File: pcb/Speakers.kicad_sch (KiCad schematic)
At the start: 34 parts, among them J17 Conn_03x01, U4 R_8_ADI, U7 R_8_ADI

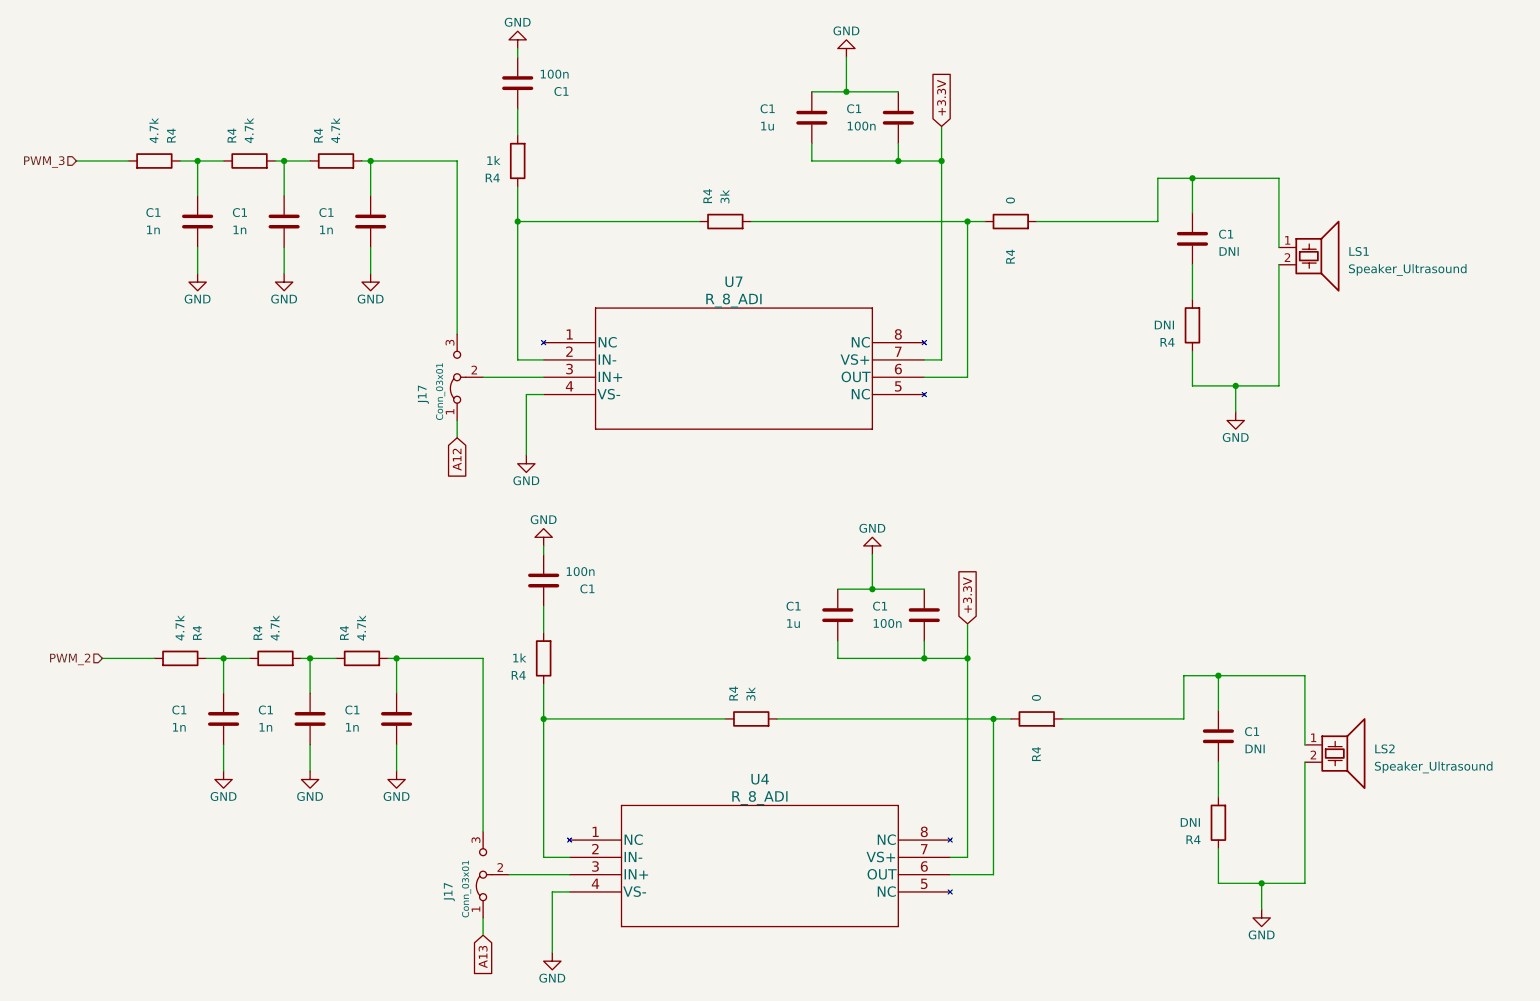
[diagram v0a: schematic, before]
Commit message: feat: Reorganize PCB project
Include all 3D step files
Refactor all folders for symbolds and footprints
Add missing datasheets
Link all symbols in KiCad projects
Rename the project to SensEdu
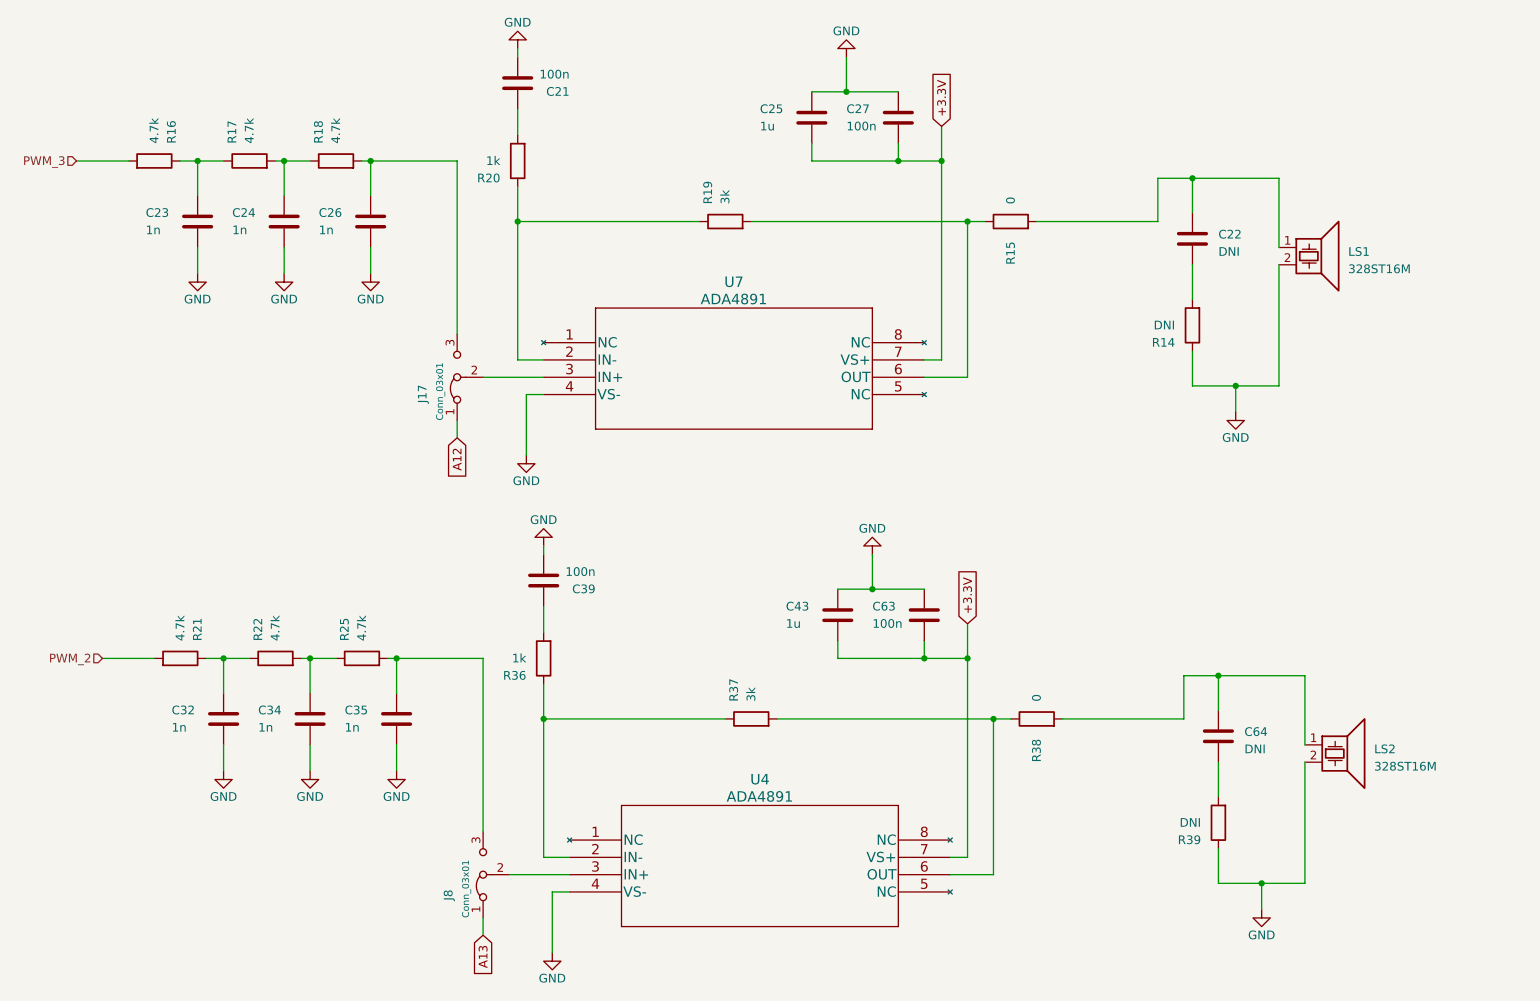
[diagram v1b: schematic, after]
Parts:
- LS1, LS2: value Speaker_Ultrasound -> 328ST16M
- U4, U7: value R_8_ADI -> ADA4891
- renumbered C1 to C21, C1 to C22, C1 to C23, C1 to C24, C1 to C25, C1 to C26, C1 to C27, C1 to C32, C1 to C34, C1 to C35, C1 to C39, C1 to C43, C1 to C63, C1 to C64, J17 to J8, R4 to R14, R4 to R15, R4 to R16, R4 to R17, R4 to R18, R4 to R19, R4 to R20, R4 to R21, R4 to R22, R4 to R25, R4 to R36, R4 to R37, R4 to R38, R4 to R39

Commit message: feat: Fix DRC errors and warnings
Updated footprint links
Updated schematic symbol for LT1790 to remove warnings
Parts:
- LS1, LS2: footprint Speaker:328ST16M_Speaker -> SensEdu:328ST16M_Speaker
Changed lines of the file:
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@@
 			)
 		)
-		(property "Footprint" "Speaker:328ST16M_Speaker"
+		(property "Footprint" "SensEdu:328ST16M_Speaker"
 			(at 209.931 126.365 0)
 			(effects
@@
 			)
 		)
-		(property "Footprint" "Speaker:328ST16M_Speaker"
+		(property "Footprint" "SensEdu:328ST16M_Speaker"
 			(at 206.121 53.34 0)
 			(effects
